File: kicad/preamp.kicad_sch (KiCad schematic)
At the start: 18 parts, among them Q1 MMBF5457, Q2 MMBF5457

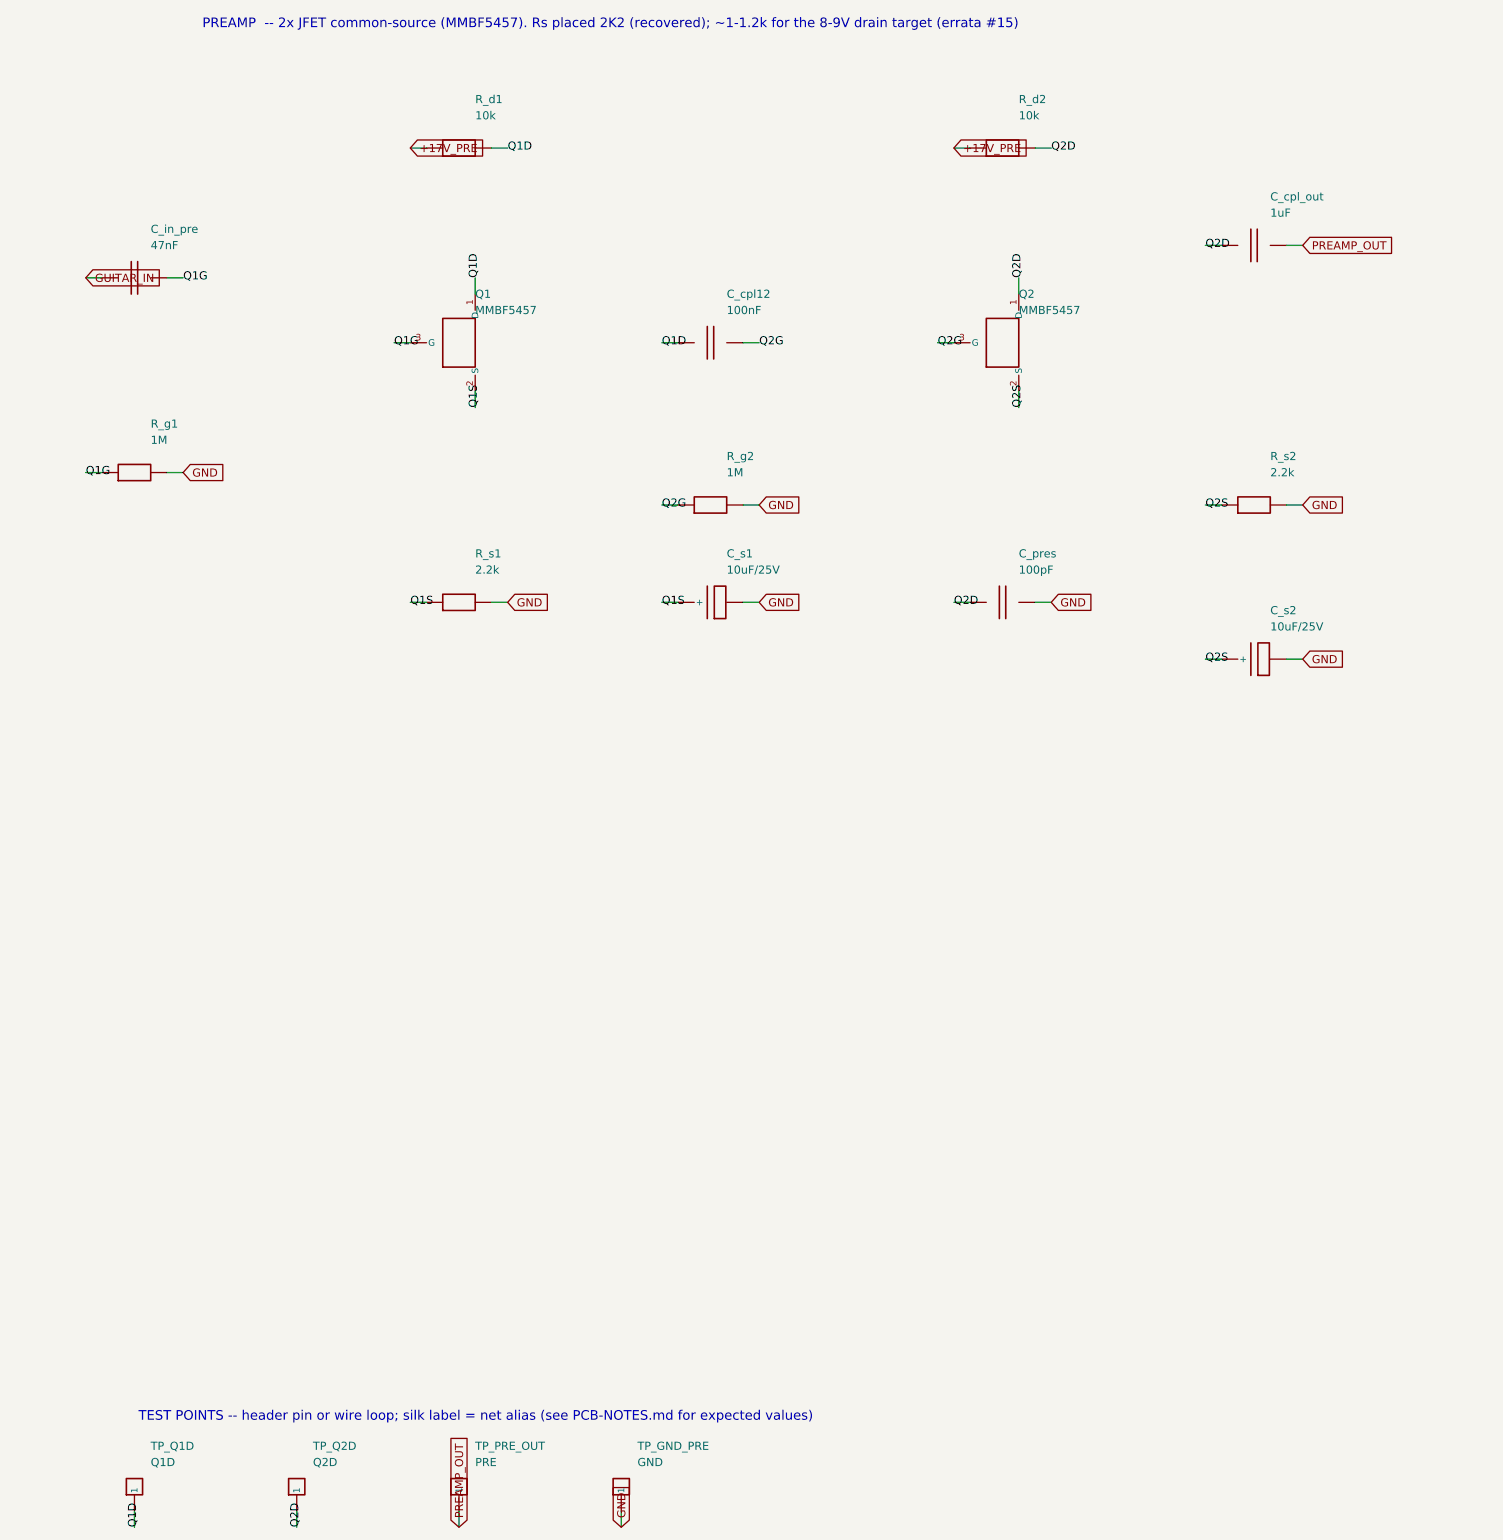
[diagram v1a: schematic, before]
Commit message: Four-layer boards, no routes through footprints, rules by impedance, RF stoppers
Both boards move to a 4-layer stack (JLC04161H-7628): F.Cu signal, In1 solid GND
plane, In2 inner signal layer, B.Cu signal + shield-only GND pour, locked perimeter
GND stitching vias every 15 mm. Outer traces sit 0.21 mm from the plane instead of
1.5 mm; the long runs live on In2 under the plane and the outer layers carry escapes.

- No routes through footprints: gen_pcb writes keepout rule areas (kp_<ref>, tracks;
  vias too under SMD parts; component side) between every part's pads -- pin-to-pin
  strips and the body between rows -- with same-net pin gaps exempt and power-only
  parts exempt. 155 / 147 areas. Freerouting gets them as keepouts, KiCad DRC checks.
- Rules by impedance: new HiZ net class (0.3 mm; gates, RF nodes, tone ladder and
  wipers, LFO timing, MRB tank, PA + input), Default = low-Z signal, Power 1.0 mm,
  HighCurrent 1.5 mm, TankDrive; .kicad_dru: HighCurrent >= 0.6 mm from any signal
  trace, tank drive >= 0.8 mm from the return (SMD 0.4 / 0.6), tracks and vias only;
  route_board hands the router the same per-class clearances.
- RF stoppers R_rf1/C_rf1 (1k + 100 pF) at Q1's gate and R_rf2/C_rf2 at the recovery
  JFET's gate (the guitar and tank cables are the antennas). Noise floor unchanged.
- route_board: strips the plane layer from the DSN (Freerouting 1.9 ignores
  (active off) and routed 7 m of copper on the planes; typed as a power layer it
  treated every through-hole pad as connected), routes inner signal layers, per-board
  class clearances, 4-layer defaults.
- SMD board 170x100 mm, 1.2 mm gap (was 155x90 / 0.5): with the keepouts every SMD
  ground / rail pad needs a via beside it and none fitted; smaller SMD rail vias.
  THT gap 1.6 mm. Placer: gaps are the routing channels now.
- Crosstalk audit knows the 4-layer geometry; cost model notes the 4-layer PCB.

Routing: THT 218/226, 0 DRC errors, 0 rule hits; SMD 216/226, 1 starved thermal.
Crosstalk aft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
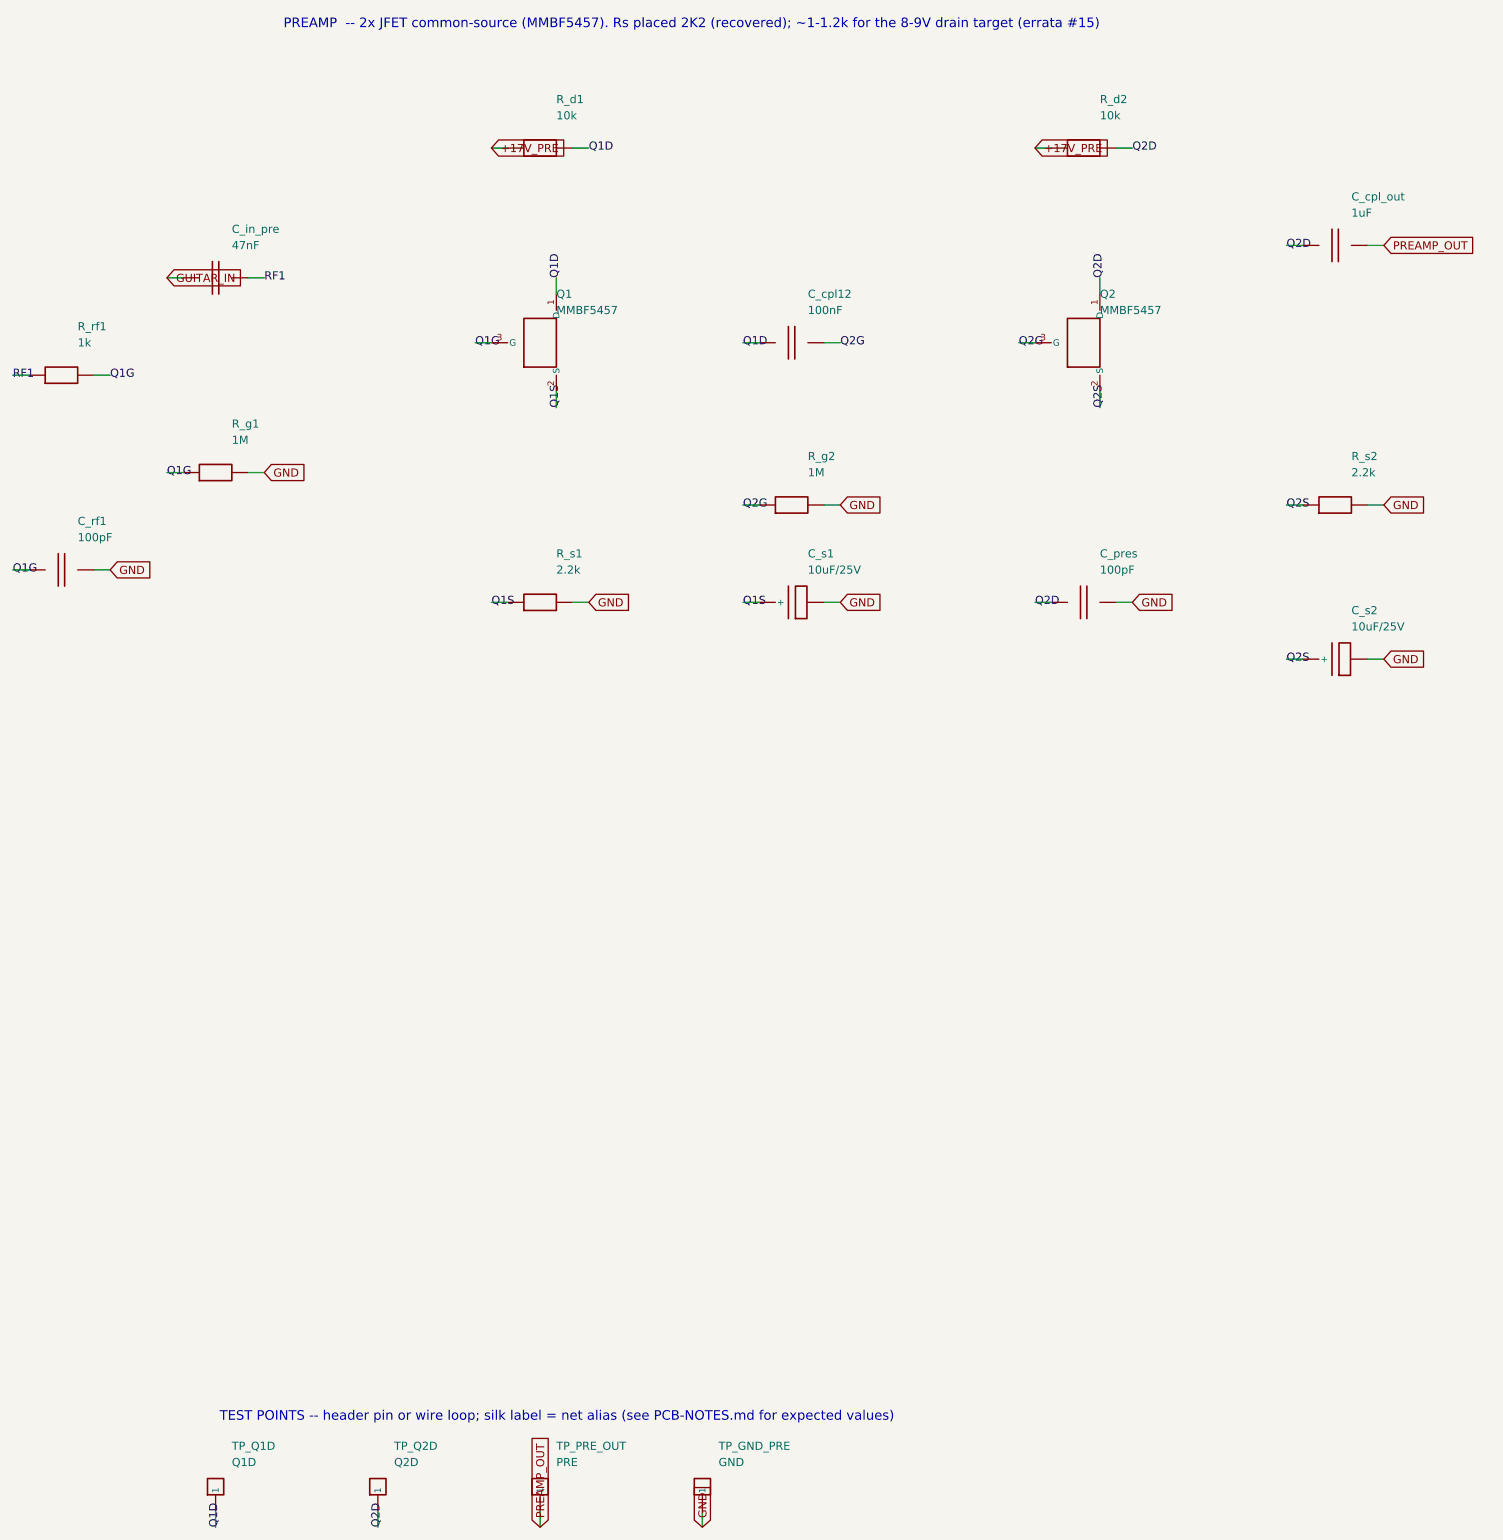
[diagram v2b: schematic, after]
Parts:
- added C_rf1: 100pF, Capacitor_THT:C_Disc_D7.5mm_W2.5mm_P5.00mm, symbol cr_primitives:C
- added R_rf1: 1k, Resistor_THT:R_Axial_DIN0207_L6.3mm_D2.5mm_P5.08mm_Vertical, symbol cr_primitives:R
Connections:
- net GND: now also C_rf1.2
- net Q1G: now also C_rf1.1, R_rf1.2; no longer C_in_pre.2
- new net RF1: C_in_pre.2, R_rf1.1
